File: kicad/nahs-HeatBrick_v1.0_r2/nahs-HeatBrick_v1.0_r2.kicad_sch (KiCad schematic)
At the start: 62 parts, among them IC1 ESP12S, IC2 ATTINY414, J2 AKL 101-02, J3 AKL 101-02, Q1 BSS138, Q3 BS170, SW1 KMR_231_G_LFS, SW2 SSSS820101, SW3 SW_DIP_x04, SW4 Taster_3301, SW5 Taster_4545, U1 MCP1700-3302, U2 LM1086_IT5,0

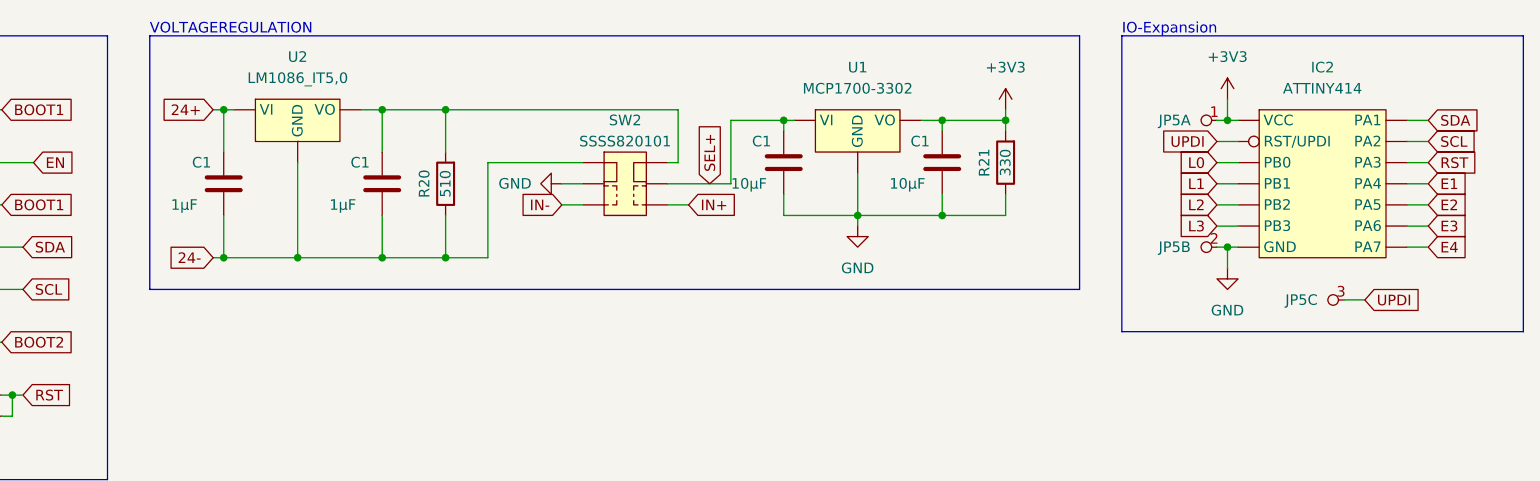
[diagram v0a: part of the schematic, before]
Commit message: v1.0 R2 Board started by removing first design flaw
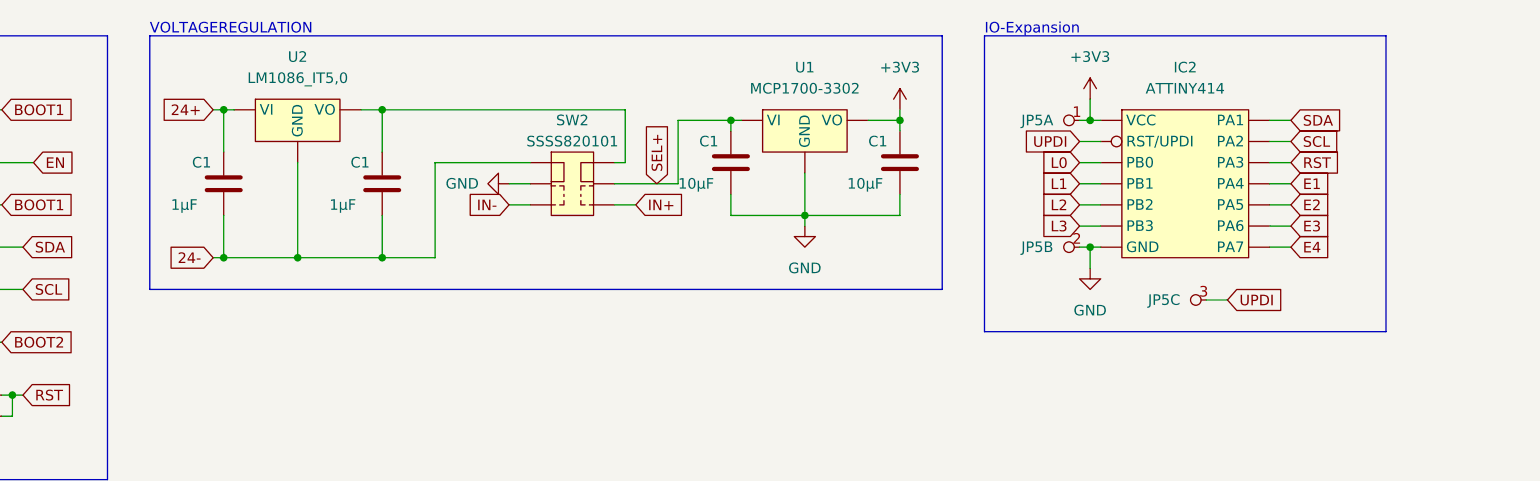
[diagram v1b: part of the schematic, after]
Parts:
- removed R20: 510, no_common:R_0603_1608Metric, symbol Device:R
- removed R21: 330, no_common:R_0603_1608Metric, symbol Device:R
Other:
- moved on the sheet: C1, IC2, JP5A, JP5B, JP5C, SW2, U1

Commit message: v1.0 R2 Board done
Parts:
- C1: Storage MAG4 -> MAGX
- U2: value LM1086_IT5,0 -> PXO7805-500-S; footprint Package_TO_SOT_THT:TO-220-3_Vertical -> no_common:PXO7805-500-S; symbol no_common:LM1086_IT5,0 -> no_common:PXO7805-500-S; Handsolder true -> (none); Storage SK1 1x4 -> SK2 2x2; StorageDesc LM1086 IT5,0 -> PXO7805-500-S
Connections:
- net 24+: now also U2.1 (VI); no longer U2.3 (VI)
- net 24-: now also U2.2 (GND); no longer U2.1 (GND)
- net at C1.1, SW2.6: now also U2.3 (VO); no longer U2.2 (VO)
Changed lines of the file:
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@@
   )
   (symbol (lib_id "no_common:MCP1700-3302") (at 195.58 30.48 0) (unit 1)
-    (in_bom yes) (on_board yes) (fields_autoplaced)
-    (property "Reference" "U1" (id 0) (at 195.58 24.13 0))
-    (property "Value" "MCP1700-3302" (id 1) (at 195.58 26.67 0))
+    (in_bom yes) (on_board yes)
+    (property "Reference" "U1" (id 0) (at 195.58 25.4 0))
+    (property "Value" "MCP1700-3302" (id 1) (at 195.58 27.94 0))
     (property "Footprint" "no_common:SOT23" (id 2) (at 195.58 30.48 0)
       (effects (font (size 1.27 1.27)) hide)
@@
       (effects (font (size 1.27 1.27)) (justify left))
     )
-    (property "Value" "1µF" (id 1) (at 119.38 40.64 0)
+    (property "Value" "10µF" (id 1) (at 119.38 40.64 0)
       (effects (font (size 1.27 1.27)) (justify left))
     )
@@
     (pin "3")
   )
-  (symbol (lib_id "no_common:LM1086_IT5,0") (at 134.62 29.21 0) (unit 1)
-    (in_bom yes) (on_board yes) (fields_autoplaced)
-    (property "Reference" "U2" (id 0) (at 134.62 22.86 0))
-    (property "Value" "LM1086_IT5,0" (id 1) (at 134.62 25.4 0))
-    (property "Footprint" "Package_TO_SOT_THT:TO-220-3_Vertical" (id 2) (at 134.62 39.37 0)
+  (symbol (lib_id "no_common:PXO7805-500-S") (at 134.62 29.21 0) (unit 1)
+    (in_bom yes) (on_board yes)
+    (property "Reference" "U2" (id 0) (at 134.62 24.13 0))
+    (property "Value" "PXO7805-500-S" (id 1) (at 134.62 26.67 0))
+    (property "Footprint" "no_common:PXO7805-500-S" (id 2) (at 134.62 39.37 0)
       (effects (font (size 1.27 1.27)) hide)
     )
@@
       (effects (font (size 1.27 1.27)) hide)
     )
-    (property "Storage" "SK1 1x4" (id 4) (at 134.62 29.21 0)
-      (effects (font (size 1.27 1.27)) hide)
-    )
-    (property "StorageDesc" "LM1086 IT5,0" (id 5) (at 134.62 29.21 0)
-      (effects (font (size 1.27 1.27)) hide)
-    )
-    (property "Handsolder" "true" (id 6) (at 134.62 29.21 0)
+    (property "Storage" "SK2 2x2" (id 4) (at 134.62 29.21 0)
+      (effects (font (size 1.27 1.27)) hide)
+    )
+    (property "StorageDesc" "PXO7805-500-S" (id 5) (at 134.62 29.21 0)
       (effects (font (size 1.27 1.27)) hide)
     )
@@
       (effects (font (size 1.27 1.27)) (justify left))
     )
-    (property "Value" "1µF" (id 1) (at 138.43 40.64 0)
+    (property "Value" "22µF" (id 1) (at 138.43 40.64 0)
       (effects (font (size 1.27 1.27)) (justify left))
     )
@@
       (effects (font (size 1.27 1.27)) hide)
     )
-    (property "Storage" "MAG4" (id 7) (at 144.78 38.1 0)
+    (property "Storage" "MAGX" (id 7) (at 144.78 38.1 0)
       (effects (font (size 1.27 1.27)) hide)
     )
@@
     )
     (path "/8bb1e2be-a1fe-43f5-ac03-8b2c86c45b89"
-      (reference "C1") (unit 1) (value "1µF") (footprint "no_common:C_0805_2012Metric")
+      (reference "C1") (unit 1) (value "10µF") (footprint "no_common:C_0805_2012Metric")
     )
     (path "/f8b26346-9941-4799-8274-7d22e70e82fd"
@@
     )
     (path "/df5bac45-1cc0-4060-af71-d91595776925"
-      (reference "C4") (unit 1) (value "1µF") (footprint "no_common:C_0805_2012Metric")
+      (reference "C4") (unit 1) (value "22µF") (footprint "no_common:C_0805_2012Metric")
     )
     (path "/1372e3a8-a100-4e9c-aa5b-b6736a9a0317"
@@
     )
     (path "/d18c44b4-abf4-4d82-a8d4-4be7d793eaf5"
-      (reference "U2") (unit 1) (value "LM1086_IT5,0") (footprint "Package_TO_SOT_THT:TO-220-3_Vertical")
-    )
-  )
+      (reference "U2") (unit 1) (value "PXO7805-500-S") (footprint "no_common:PXO7805-500-S")
+    )
+  )
